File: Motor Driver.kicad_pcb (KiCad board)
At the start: 2 copper layers, 103.6 x 67.8 mm, 45 parts, among them CON1 AVR-ISP-6, J1 Conn_01x02, J10 Conn_01x04, J2 Conn_01x02, J3 Conn_01x04, J4 Conn_01x04, J5 Conn_01x04, J6 Conn_02x02_Odd_Even, J7 Conn_01x02, J8 Conn_01x02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

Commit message: Added Isolation
Added an Optoisolator to isolate the input signal
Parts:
- added J11: Conn_01x02, Pin_Headers:Pin_Header_Straight_1x02_Pitch2.54mm, F.Cu at (95.6, 117.7)
- added R14: 200, Resistors_THT:R_Axial_DIN0207_L6.3mm_D2.5mm_P7.62mm_Horizontal, F.Cu at (103.3, 111.7)
- added R15: 200, Resistors_THT:R_Axial_DIN0207_L6.3mm_D2.5mm_P7.62mm_Horizontal, F.Cu at (116.8, 121.9)
- added R16: 200, Resistors_THT:R_Axial_DIN0207_L6.3mm_D2.5mm_P7.62mm_Horizontal, F.Cu at (109.9, 112.4)
- added U2: PC817, Housings_DIP:DIP-4_W7.62mm, F.Cu at (103.3, 115.1)
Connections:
- net Net-(J1-Pad2) renamed /INPUT_L
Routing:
- net +5V: track 169.9 -> 197.5 mm
- net Net-(J11-Pad1): track 0.00 -> 7.62 mm
- net /INPUT_L: track 12.5 -> 19.9 mm
- net Net-(R14-Pad1): track 0.00 -> 3.43 mm
- net Net-(J11-Pad2): track 0.00 -> 3.43 mm
- net Net-(R16-Pad1): track 0.00 -> 3.13 mm
- net Net-(C9-Pad2): track 75.7 -> 77.6 mm
- net VCC: track 126.0 -> 127.5 mm
- net Net-(C10-Pad2): track 87.3 -> 85.8 mm
- net Net-(Q2-Pad1): track 19.9 -> 21.0 mm
- net /IN1: track 19.7 -> 20.5 mm
- net Net-(CON1-Pad1): track 16.0 -> 15.3 mm
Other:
- board text added: "1"

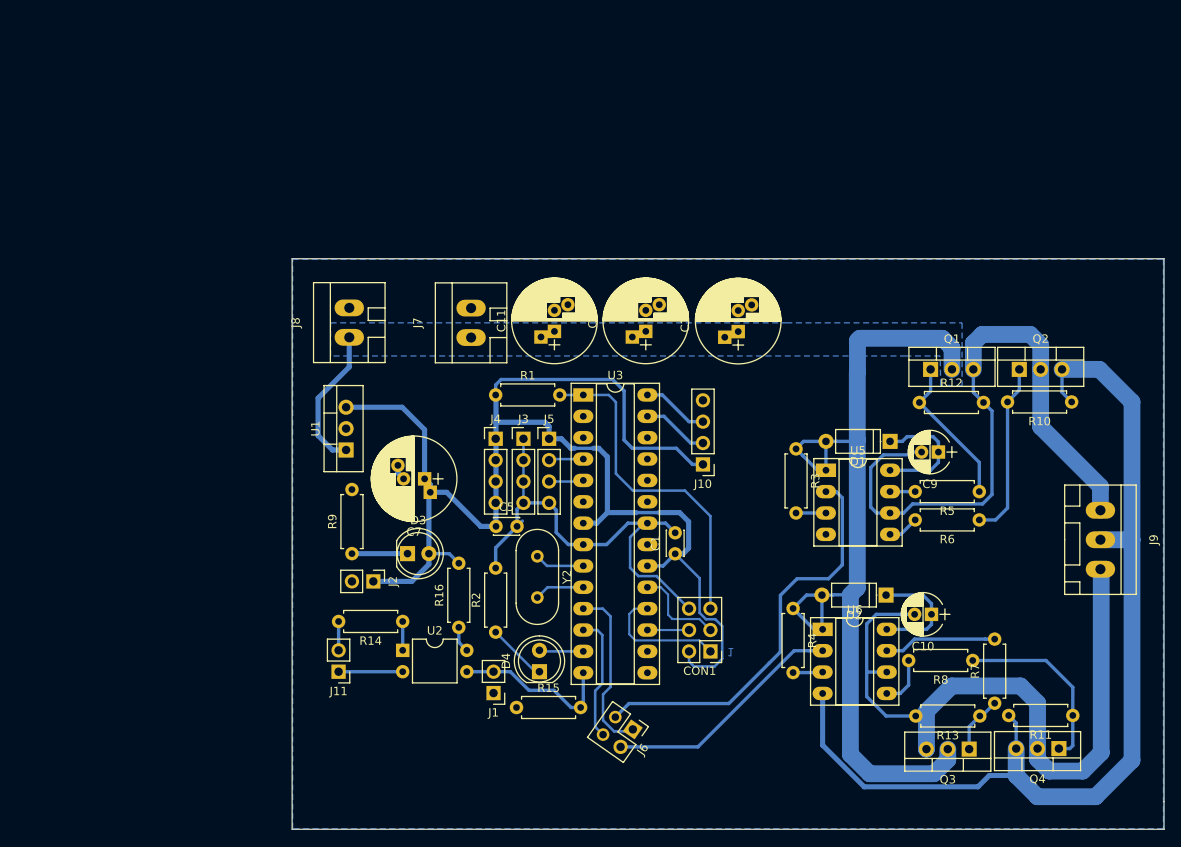
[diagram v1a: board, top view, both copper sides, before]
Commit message: Seecond iteration
Modified according to the new motor acquired
Fixed errors in the SCH->Added gate diodes
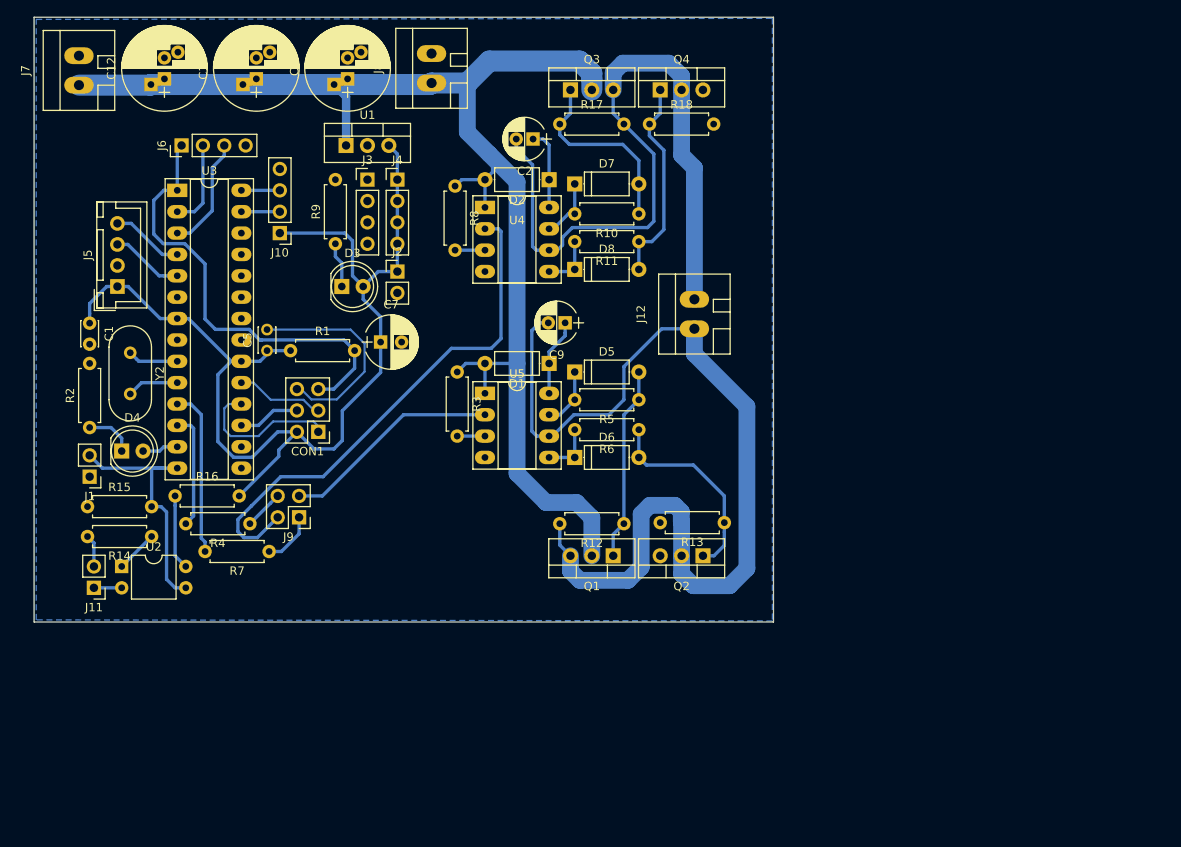
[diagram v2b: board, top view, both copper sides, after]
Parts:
- removed C10: CP_Small, Capacitors_THT:CP_Radial_D5.0mm_P2.00mm
- removed U6: IR2104, Housings_DIP:DIP-8_W7.62mm_Socket_LongPads
- added C2: CP_Small, Capacitors_THT:CP_Radial_D5.0mm_P2.00mm, F.Cu at (118.7, 54.4)
- added D5: D, Diodes_THT:D_A-405_P7.62mm_Horizontal, F.Cu at (123.7, 82.0)
- added D6: D, Diodes_THT:D_A-405_P7.62mm_Horizontal, F.Cu at (123.7, 92.2)
- added D7: D, Diodes_THT:D_A-405_P7.62mm_Horizontal, F.Cu at (123.7, 59.7)
- added D8: D, Diodes_THT:D_A-405_P7.62mm_Horizontal, F.Cu at (123.7, 69.8)
- added J12: Conn_01x02, Connectors_WAGO:WAGO_734_2pin_Straight_RuggedPads, F.Cu at (137.9, 75.2)
- added R17: R_Small, Resistors_THT:R_Axial_DIN0207_L6.3mm_D2.5mm_P7.62mm_Horizontal, F.Cu at (121.9, 52.6)
- added R18: R_Small, Resistors_THT:R_Axial_DIN0207_L6.3mm_D2.5mm_P7.62mm_Horizontal, F.Cu at (132.6, 52.6)
- added U4: IR2104, Housings_DIP:DIP-8_W7.62mm_Socket_LongPads, F.Cu at (113.0, 62.5)
- C7: footprint Capacitors_THT:CP_Radial_D10.0mm_P2.50mm_P5.00mm -> Capacitors_THT:CP_Radial_D6.3mm_P2.50mm
- J5: footprint Pin_Headers:Pin_Header_Straight_1x04_Pitch2.54mm -> Connectors_JST:JST_XH_B04B-XH-A_04x2.50mm_Straight
- J6: value Conn_02x02_Odd_Even -> Conn_01x04; footprint Pin_Headers:Pin_Header_Straight_2x02_Pitch2.54mm -> Pin_Headers:Pin_Header_Straight_1x04_Pitch2.54mm
- J9: value Conn_01x03 -> Conn_02x02_Odd_Even; footprint Connectors_WAGO:WAGO_734_3pin_Straight_RuggedPads -> Pin_Headers:Pin_Header_Straight_2x02_Pitch2.54mm
- R12, R13: value R -> R_Small
- R16: value 200 -> 1
- moved J9 95.3 mm to (90.9, 99.3), turned to 180 degrees
- moved Q3 91.6 mm to (123.2, 48.5), turned to 0 degrees
- moved Q4 91.5 mm to (133.9, 48.5), turned to 0 degrees
- moved R7 88.1 mm to (87.4, 103.4), turned to 180 degrees
- moved J6 87.7 mm to (77.0, 55.1), turned to 90 degrees
- moved R8 83.5 mm to (109.5, 59.9), turned to 270 degrees
- moved R11 76.4 mm to (131.3, 66.5)
- moved C1 74.8 mm to (66.0, 76.2), turned to 270 degrees
- moved C12 74.5 mm to (74.9, 47.2)
- moved R4 65.3 mm to (85.1, 100.1), turned to 180 degrees
- moved D2 63.6 mm to (120.7, 59.2)
- moved J10 57.3 mm to (88.6, 65.5)
- moved R15 56.3 mm to (65.8, 98.0)
- moved D4 56.2 mm to (69.8, 91.4), turned to 0 degrees
- moved R10 56.1 mm to (131.3, 63.2)
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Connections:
- J5 pad 2: Net-(J5-Pad2) -> GND
- J5 pad 4: GND -> Net-(J5-Pad4)
- J6 pad 1: /IN1 -> /RST
- J6 pad 4: /IN2 -> GND
- J9 pad 1: Net-(C9-Pad2) -> Net-(J9-Pad1)
- J9 pad 2: GND -> Net-(J9-Pad2)
- J9 pad 3: Net-(C10-Pad2) -> Net-(J9-Pad3)
- Q2 pad 1: Net-(Q2-Pad1) -> Net-(D6-Pad2)
- Q3 pad 1: Net-(Q3-Pad1) -> Net-(D7-Pad2)
- Q3 pad 3: Net-(C10-Pad2) -> Net-(C2-Pad2)
- Q4 pad 1: Net-(Q4-Pad1) -> Net-(D8-Pad2)
- Q4 pad 2: Net-(C10-Pad2) -> Net-(C2-Pad2)
- R10 pad 1: GND -> Net-(D7-Pad2)
- R10 pad 2: Net-(Q2-Pad1) -> Net-(D7-Pad1)
- R11 pad 1: Net-(Q4-Pad1) -> Net-(D8-Pad2)
- R11 pad 2: GND -> Net-(D8-Pad1)
- R13 pad 1: Net-(Q3-Pad1) -> Net-(D6-Pad2)
- R13 pad 2: Net-(C10-Pad2) -> GND
- R4 pad 1: VCC -> Net-(J9-Pad4)
- R4 pad 2: Net-(R4-Pad2) -> /IN2
- R6 pad 1: Net-(Q2-Pad1) -> Net-(D6-Pad2)
- R7 pad 1: Net-(Q3-Pad1) -> Net-(J9-Pad1)
- R7 pad 2: Net-(R7-Pad2) -> /IN1
- R8 pad 1: Net-(Q4-Pad1) -> VCC
- U3 pad 15: Net-(U3-Pad15) -> (no net)
- U3 pad 16: Net-(U3-Pad16) -> (no net)
- U3 pad 2: Net-(U3-Pad2) -> Net-(J6-Pad2)
- U3 pad 21: Net-(U3-Pad21) -> (no net)
- U3 pad 23: Net-(U3-Pad23) -> (no net)
- U3 pad 24: Net-(U3-Pad24) -> (no net)
- U3 pad 25: Net-(U3-Pad25) -> (no net)
- U3 pad 26: Net-(U3-Pad26) -> (no net)
- U3 pad 3: Net-(U3-Pad3) -> Net-(J6-Pad3)
- U3 pad 4: Net-(J5-Pad2) -> Net-(J5-Pad4)
- U3 pad 6: Net-(U3-Pad6) -> (no net)
- U5 pad 2: Net-(J6-Pad3) -> Net-(J9-Pad3)
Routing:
- net GND: track 174.6 -> 25.9 mm
- net Net-(C2-Pad2): track 0.00 -> 86.2 mm
- net Net-(C10-Pad2): track 85.8 -> 0.00 mm
- net +5V: track 197.5 -> 126.5 mm
- net Net-(J9-Pad2): track 0.00 -> 62.4 mm
- net Net-(C9-Pad2): track 77.6 -> 117.0 mm
- net VCC: track 127.5 -> 164.5 mm
- net Net-(J6-Pad3): track 48.6 -> 13.6 mm
- net Net-(J9-Pad3): track 0.00 -> 26.1 mm
- net Net-(D8-Pad2): track 0.00 -> 24.7 mm
- net Net-(D6-Pad2): track 0.00 -> 24.3 mm
- net Net-(D7-Pad2): track 0.00 -> 22.9 mm
- net Net-(Q4-Pad1): track 21.9 -> 0.00 mm
- net Net-(Q2-Pad1): track 21.0 -> 0.00 mm
- net Net-(J6-Pad2): track 28.8 -> 10.3 mm
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- removed copper zone on B.Cu, net VCC
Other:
- board size 103.6 x 67.8 mm -> 87.9 x 71.9 mm
- board text removed: "1"
